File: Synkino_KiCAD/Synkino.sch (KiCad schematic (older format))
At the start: 69 parts

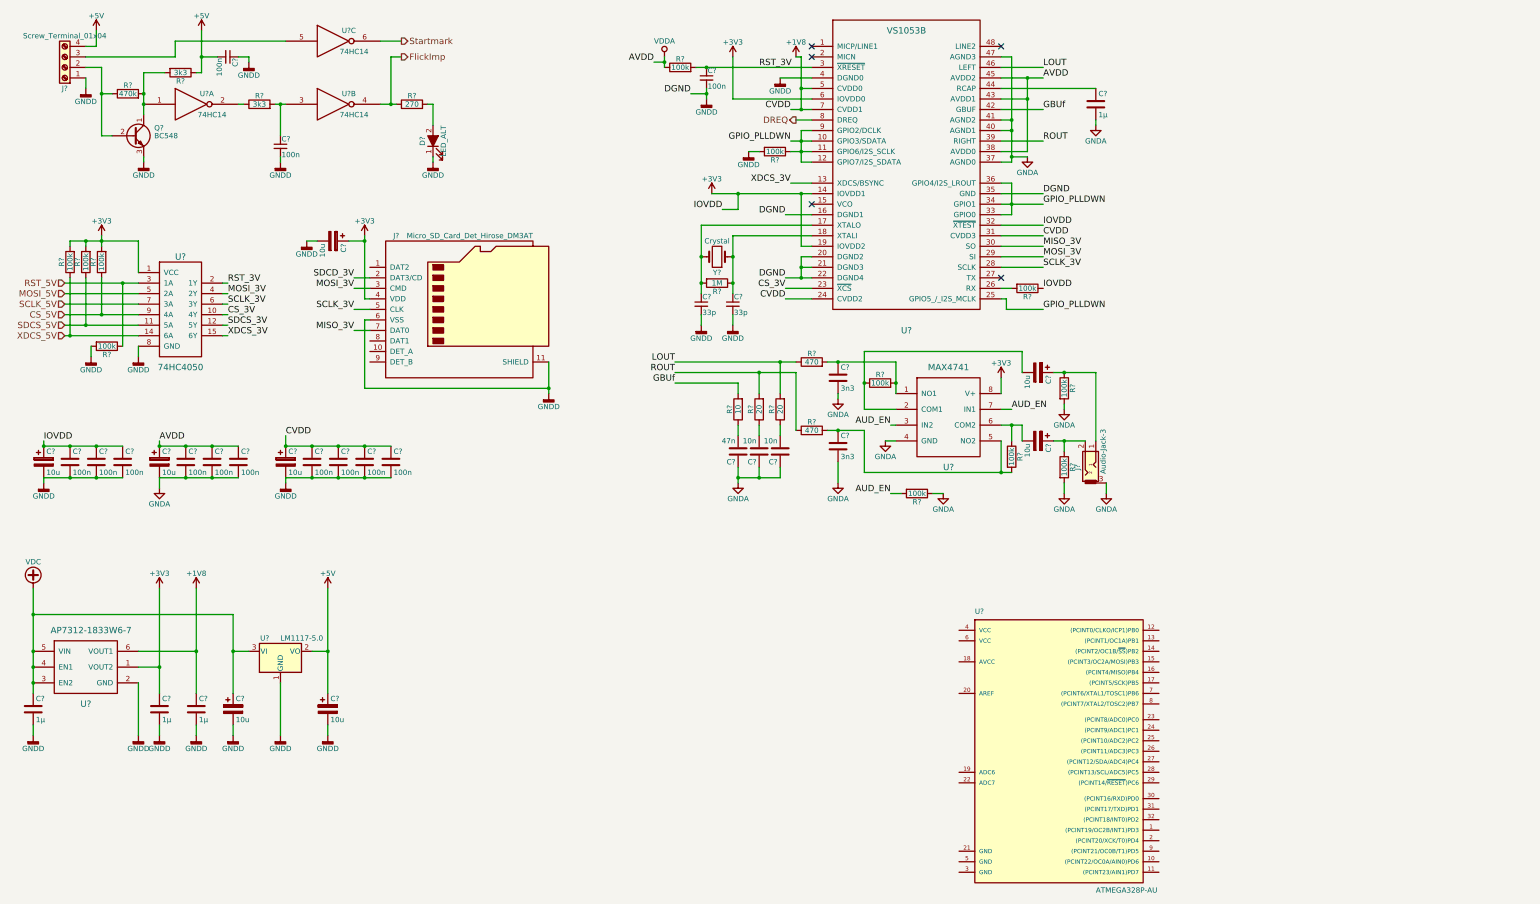
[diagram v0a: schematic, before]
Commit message: Adding 328P for Audio
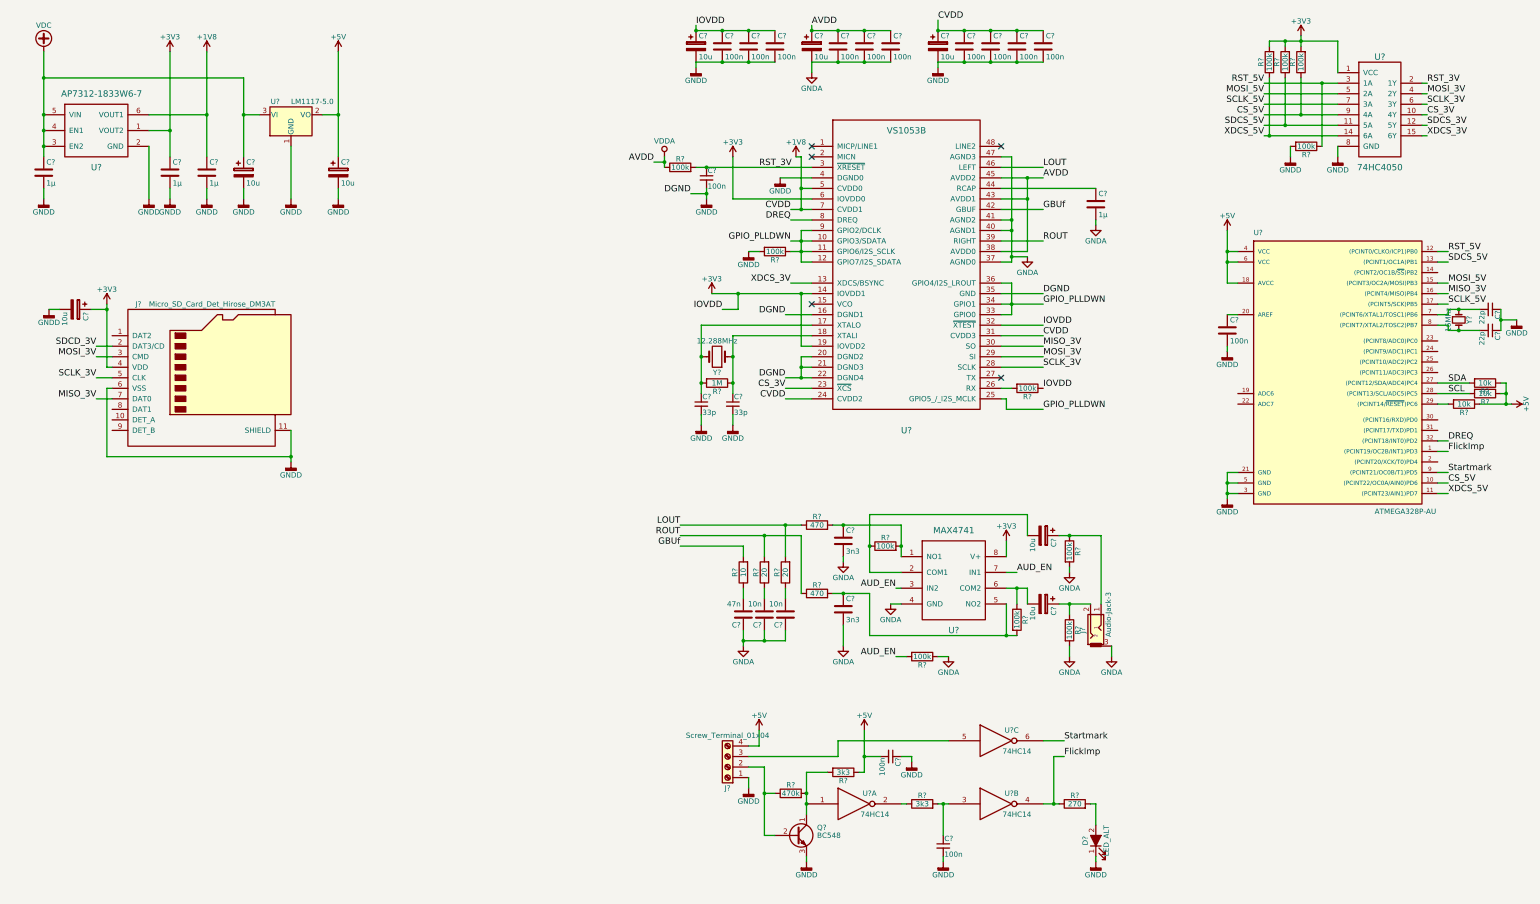
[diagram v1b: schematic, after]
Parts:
- added C?: 100n, symbol C
- added C? (x2): 22p, symbol C_Small
- added R? (x3): 10k, symbol R
- added Y?: 16Mhz, symbol Crystal_Small
- Y?: value Crystal -> 12.288MHz
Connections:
- net +5V: now also U?.18 (AVCC), U?.4 (VCC), U?.6 (VCC), R?.1, R?.1, R?.1
- net CS_5V: now also U?.10 ((PCINT22/OC0A/AIN0)PD6)
- net DREQ: now also U?.32 ((PCINT18/INT0)PD2)
- net FlickImp: now also U?.1 ((PCINT19/OC2B/INT1)PD3)
- net GNDD: now also U?.21 (GND), U?.3 (GND), U?.5 (GND), C?.1, C?.1, C?.2
- net MISO_3V: now also U?.16 ((PCINT4/MISO)PB4)
- net MOSI_5V: now also U?.15 ((PCINT3/OC2A/MOSI)PB3)
- net RST_5V: now also U?.12 ((PCINT0/CLKO/ICP1)PB0)
- net SCLK_5V: now also U?.17 ((PCINT5/SCK)PB5)
- net SDCS_5V: now also U?.13 ((PCINT1/OC1A)PB1)
- net Startmark: now also U?.9 ((PCINT21/OC0B/T1)PD5)
- net XDCS_5V: now also U?.11 ((PCINT23/AIN1)PD7)
- net at U?.20 (AREF): now also C?.1
- net SDA: now reaches U?.27 ((PCINT12/SDA/ADC4)PC4)
- net SDA: now also R?.2
- net SCL: now reaches U?.28 ((PCINT13/SCL/ADC5)PC5)
- net SCL: now also R?.2
- net at U?.29 ((PCINT14/~RESET~)PC6): now also R?.2
- net at U?.7 ((PCINT6/XTAL1/TOSC1)PB6): now also C?.2, Y?.1
- net at U?.8 ((PCINT7/XTAL2/TOSC2)PB7): now also C?.2, Y?.2
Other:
- moved on the sheet: C?, D?, J?, Q?, R?, U?, U?A, U?B, U?C, Y?

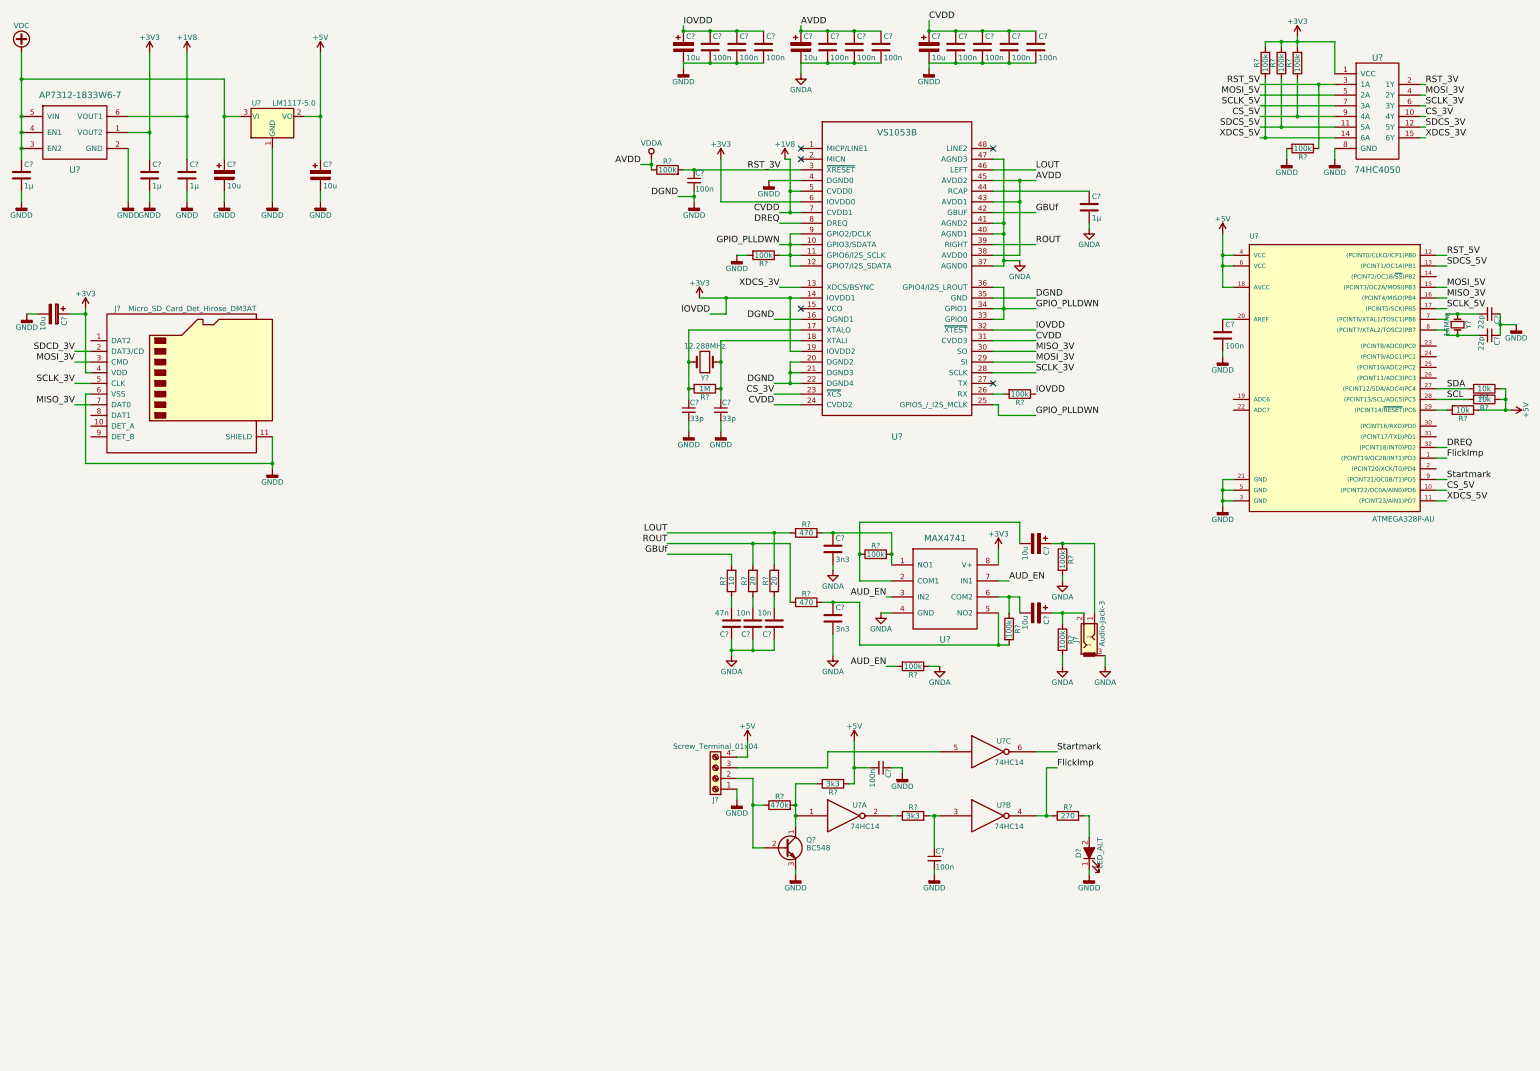
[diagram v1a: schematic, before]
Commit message: Adding 2nd 328 and Control Components
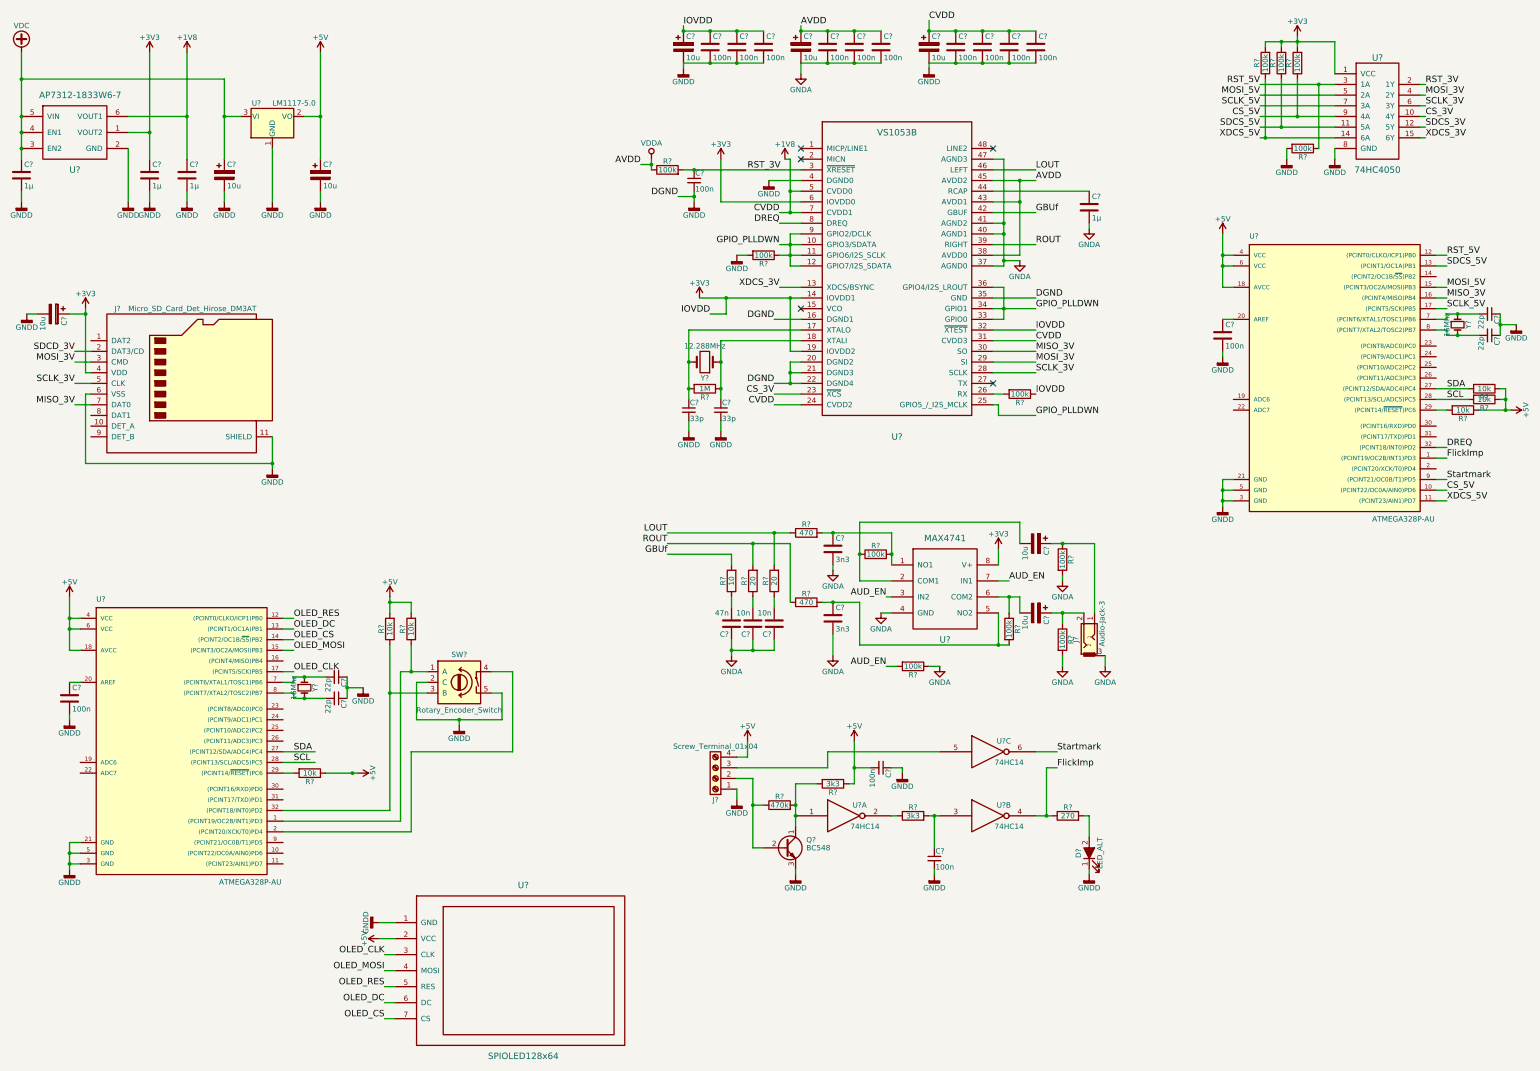
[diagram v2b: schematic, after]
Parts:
- added C?: 100n, symbol C
- added C? (x2): 22p, symbol C_Small
- added R? (x3): 10k, symbol R
- added SW?: Rotary_Encoder_Switch, symbol Rotary_Encoder_Switch
- added U?: SPIOLED128x64, symbol SPIOLED128x64
- added U?: ATMEGA328P-AU, Housings_QFP:TQFP-32_7x7mm_Pitch0.8mm, symbol ATMEGA328P-AU
- added Y?: 16Mhz, symbol Crystal_Small
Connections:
- net +5V: now also R?.1, R?.2, R?.2, U?.18 (AVCC), U?.2 (VCC), U?.4 (VCC), U?.6 (VCC)
- net GNDD: now also C?.1, C?.1, C?.2, SW?.2 (C), SW?.5, U?.1 (GND), U?.21 (GND), U?.3 (GND), U?.5 (GND)
- net SCL: now also U?.28 ((PCINT13/SCL/ADC5)PC5)
- net SDA: now also U?.27 ((PCINT12/SDA/ADC4)PC4)
- new net: R?.1, SW?.3 (B), U?.32 ((PCINT18/INT0)PD2)
- new net: R?.1, SW?.1 (A), U?.1 ((PCINT19/OC2B/INT1)PD3)
- new net: SW?.4, U?.2 ((PCINT20/XCK/T0)PD4)
- new net: C?.1, U?.20 (AREF)
- new net: R?.2, U?.29 ((PCINT14/~RESET~)PC6)
- new net: C?.2, U?.7 ((PCINT6/XTAL1/TOSC1)PB6), Y?.1
- new net: C?.2, U?.8 ((PCINT7/XTAL2/TOSC2)PB7), Y?.2
- new net OLED_CLK: U?.17 ((PCINT5/SCK)PB5), U?.3 (CLK)
- new net OLED_CS: U?.14 ((PCINT2/OC1B/~SS~)PB2), U?.7 (CS)
- new net OLED_DC: U?.13 ((PCINT1/OC1A)PB1), U?.6 (DC)
- new net OLED_MOSI: U?.15 ((PCINT3/OC2A/MOSI)PB3), U?.4 (MOSI)
- new net OLED_RES: U?.12 ((PCINT0/CLKO/ICP1)PB0), U?.5 (RES)

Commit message: Schematics complete?
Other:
- note added: "Also, Sigma-Delta-Decoding to have a decent Line Signal"
- note added: "Audio Playback & DSP"
- note added: "De-Click Logic to avoid the nasty pops from RCAP"
- note added: "Level Shifter, VS1053 likes 3v3 only, Mega328 needs 5V though for 16 MHz"
- note added: "Mega328 for Control & Display"
- note added: "Mega328 providing PID and feeding DSP with uSD data"
- note added: "Power Bypass Caps, place as close to chip as possible"
- note added: "Power Supplies"
- note added: "Signal Cleanup for the two optical Sensors on the projector"
- note added: "uSD Card Reader in SPI Mode"
- moved on the sheet: C?, D?, J?, Q?, R?, U?, U?A, U?B, U?C, Y?

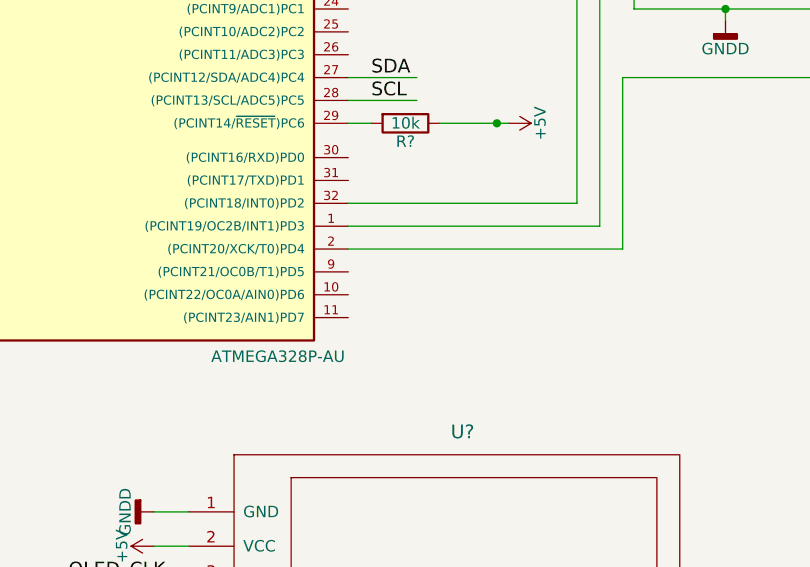
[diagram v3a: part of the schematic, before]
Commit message: Prepare for Audio_Enable
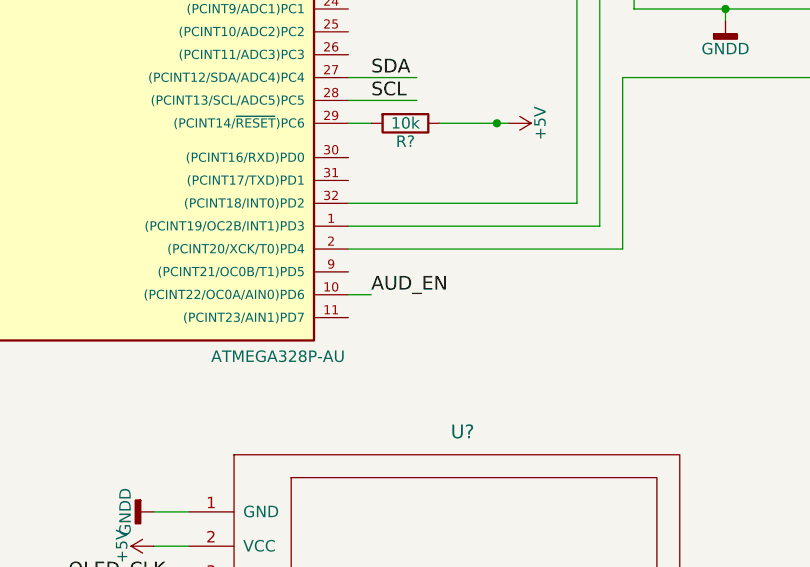
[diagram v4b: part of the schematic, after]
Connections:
- net AUD_EN: now also U?.10 ((PCINT22/OC0A/AIN0)PD6)
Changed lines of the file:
@@
 Text Notes 11250 2600 0    60   ~ 0
 Mega328 providing PID and feeding DSP with uSD data
+Text Label 3400 8500 0    60   ~ 0
+AUD_EN
+Wire Wire Line
+	3300 8500 3400 8500
 $EndSCHEMATC

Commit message: Adding ICSP connectors
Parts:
- added X? (x2): ICSP, symbol ICSP
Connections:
- net +5V: now also X?.2 (VCC), X?.2 (VCC)
- net GNDD: now also X?.6 (GND), X?.6 (GND)
- net MISO_3V: now also X?.1 (MI)
- net MOSI_5V: now also X?.4 (MO)
- net OLED_CLK: now also X?.3 (SCK)
- net SCLK_5V: now also X?.3 (SCK)
- net ~RST: now reaches R?.2, U?.29 ((PCINT14/~RESET~)PC6)
- net ~RST: now also X?.5 (RST)
- net CTRL_MISO: now reaches U?.16 ((PCINT4/MISO)PB4)
- net CTRL_MISO: now also X?.1 (MI)
- net CTRL_RST: now reaches R?.2, U?.29 ((PCINT14/~RESET~)PC6)
- net CTRL_RST: now also X?.5 (RST)
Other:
- moved on the sheet: C?, R?, SW?, U?, Y?
